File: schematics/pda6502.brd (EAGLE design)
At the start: 100 x 80 mm, 38 parts, among them IC1 74HC00D, IC2 74HC138D, IC3 DS1813-SMD, J1 CON_HEADER_2X07-PTH, U1 W65C02S, U2 W65C22S, U3 28C256, U4 UM61256AK-12

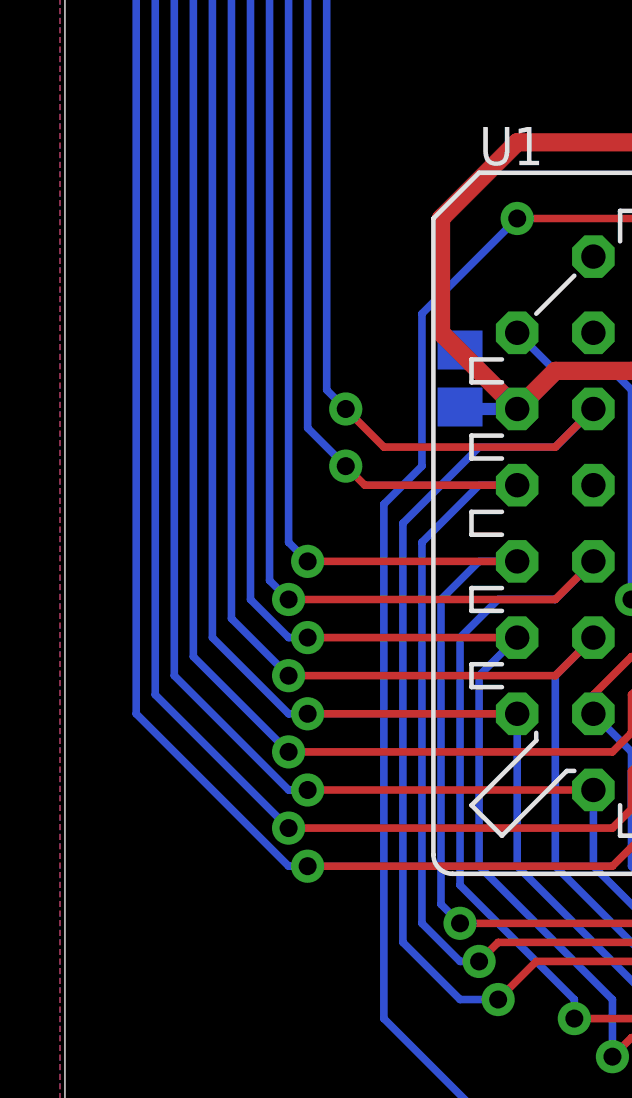
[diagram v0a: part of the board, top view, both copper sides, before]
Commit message: board: PDA6502-LOGO next to 6502.
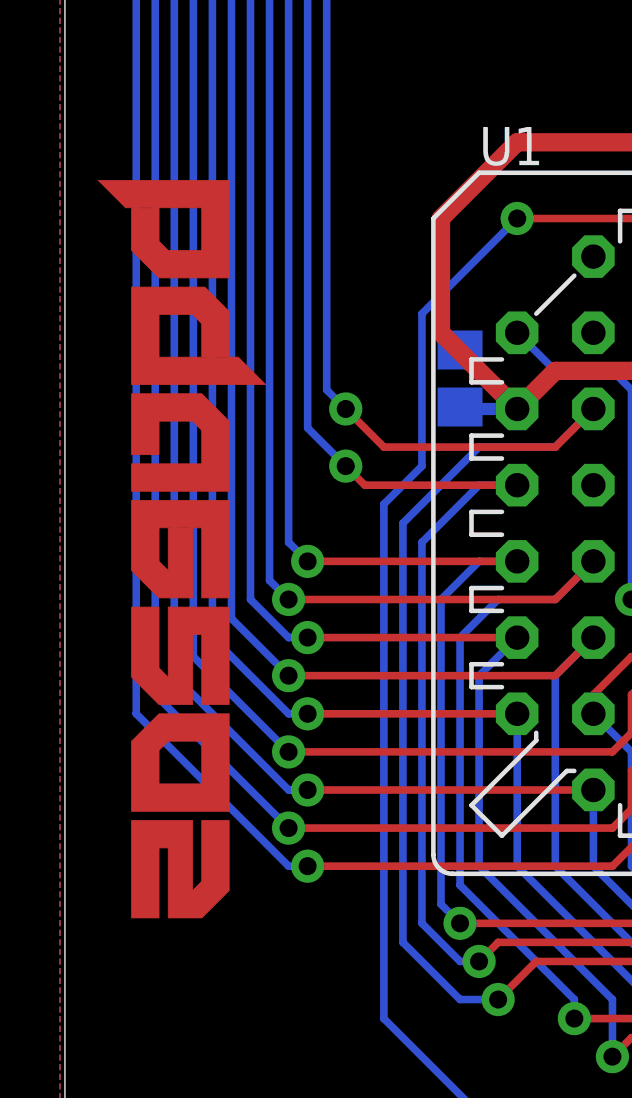
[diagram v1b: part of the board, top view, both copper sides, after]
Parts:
- added U$3: (no value), pda:PDA6502-LOGO
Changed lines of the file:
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@@
 <element name="R4" library="resistor" package="R0805" value="3.3K" x="22.86" y="24.765" rot="MR0"/>
 <element name="U$2" library="pda" package="ADA-TFT-240X230-22INCH" value="" x="67.31" y="27.94"/>
+<element name="U$3" library="pda" package="PDA6502-LOGO" value="" x="1.27" y="36.83" rot="R270"/>
 </elements>
 <signals>

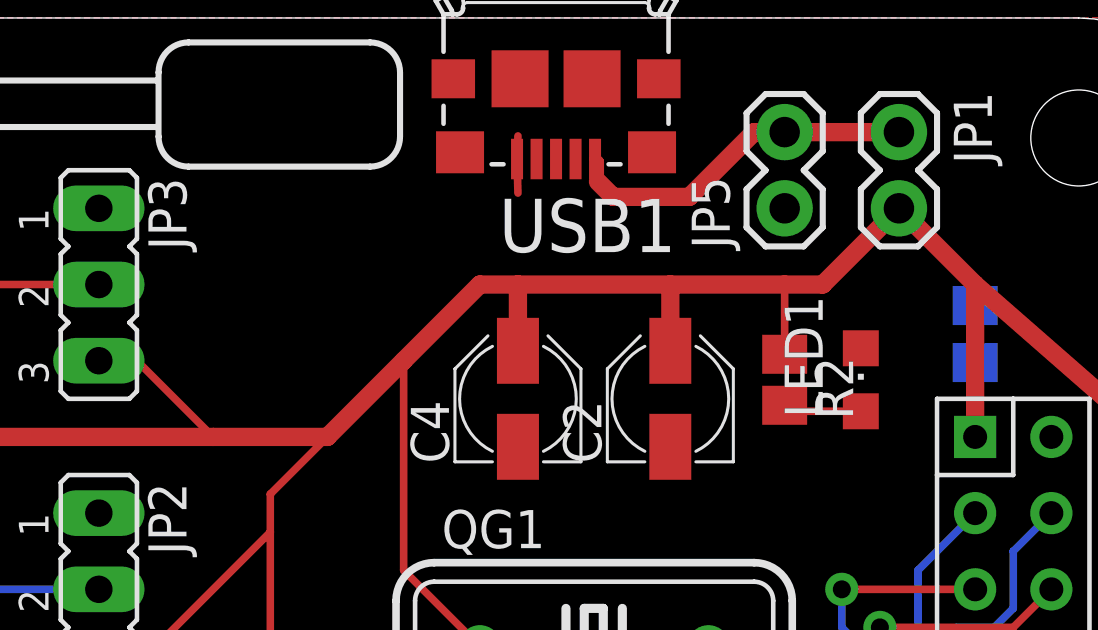
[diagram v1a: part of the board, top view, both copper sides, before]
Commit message: board: PDA6502-LOGO on bottom also; near USB connector.
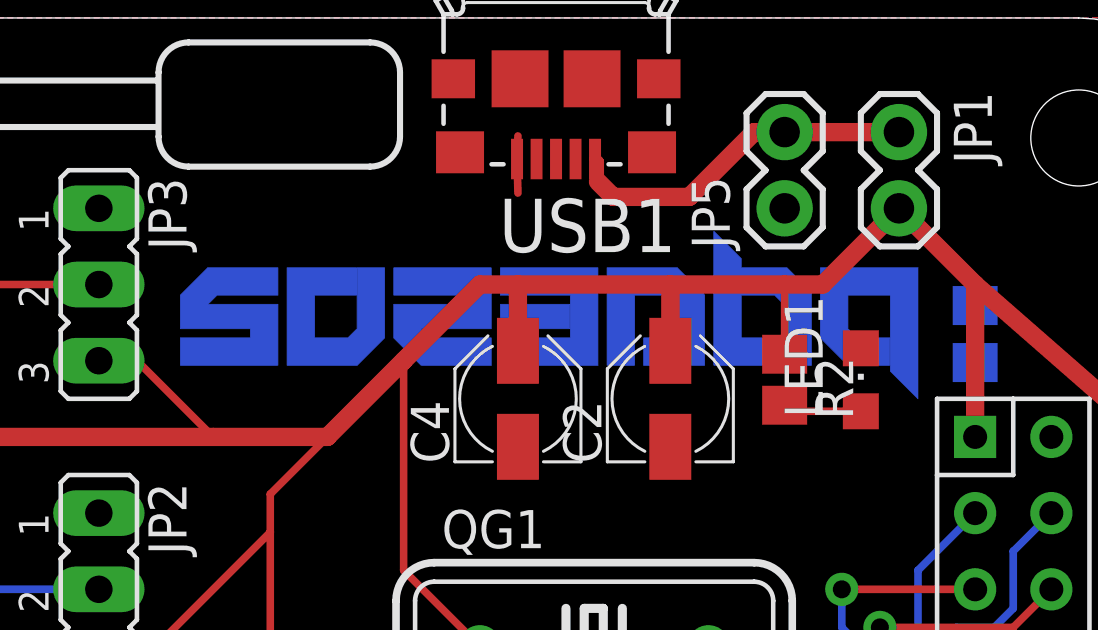
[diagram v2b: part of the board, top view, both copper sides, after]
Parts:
- added U$4: (no value), pda:PDA6502-LOGO
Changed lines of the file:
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@@
 <element name="U$2" library="pda" package="ADA-TFT-240X230-22INCH" value="" x="67.31" y="27.94"/>
 <element name="U$3" library="pda" package="PDA6502-LOGO" value="" x="1.27" y="36.83" rot="R270"/>
+<element name="U$4" library="pda" package="PDA6502-LOGO" value="" x="90.805" y="67.31" rot="MR0"/>
 </elements>
 <signals>

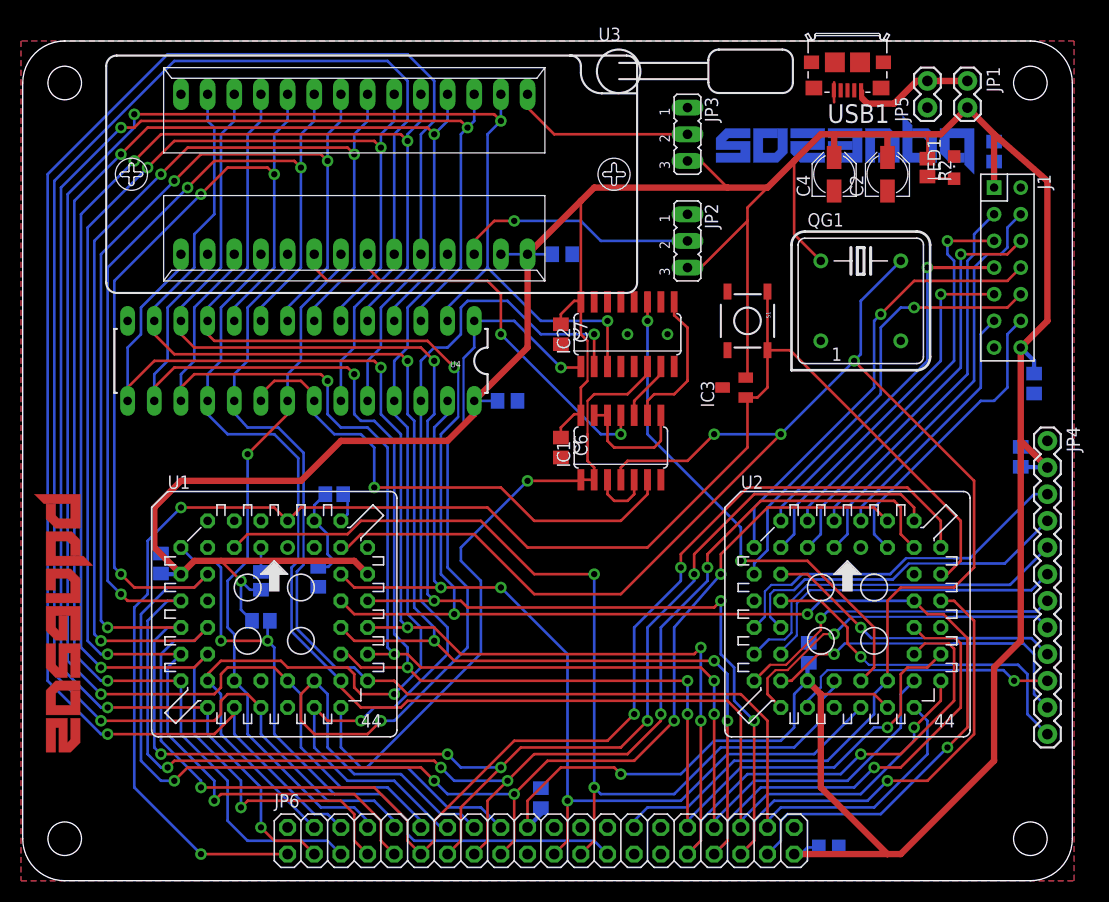
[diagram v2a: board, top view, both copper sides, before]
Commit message: schematics, board: labelling WIP, bigger caps.
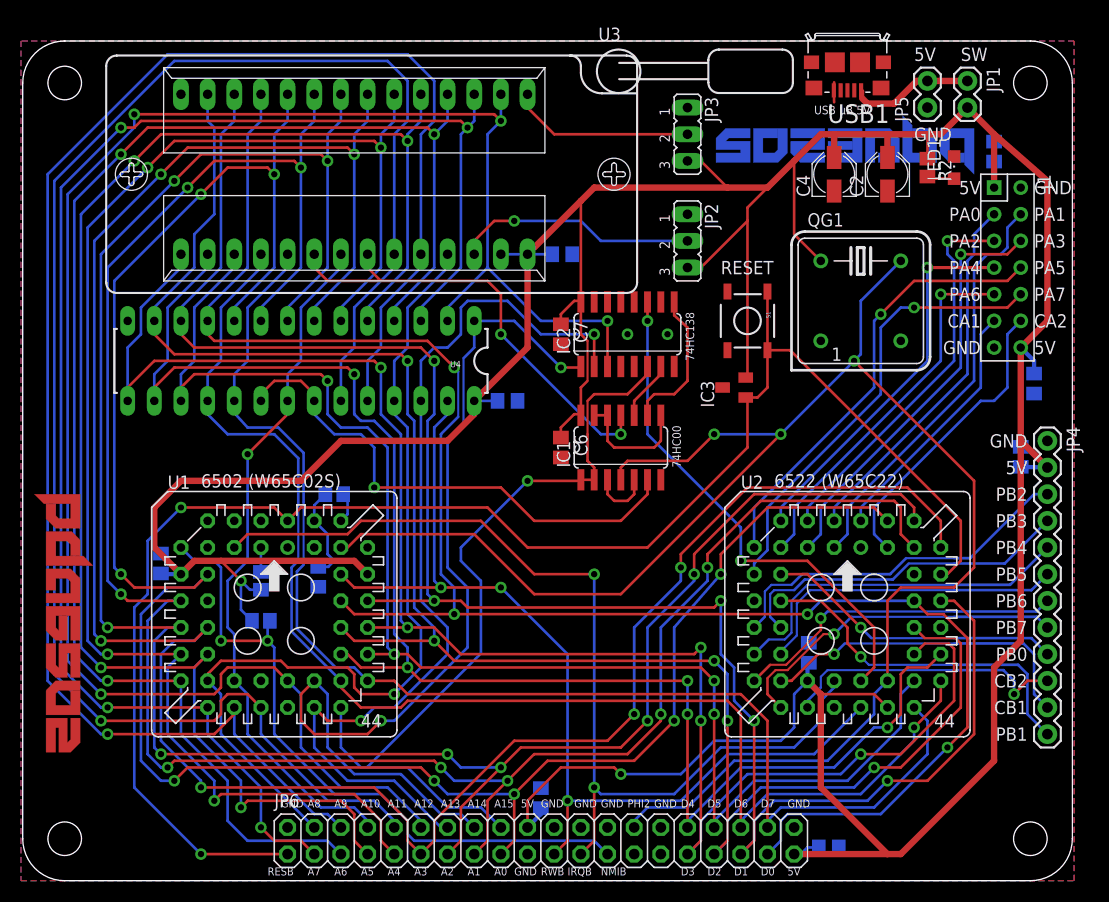
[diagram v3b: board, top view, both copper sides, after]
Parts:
- C12, C13, C14, C9: value 0.1μF -> 1μF
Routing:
- net CB2: track 25.7 -> 27.5 mm
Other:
- board text added: "5V"
- board text added: "6502 (W65C02S)"
- board text added: "6522 (W65C22)"
- board text added: "74HC00"
- board text added: "74HC138"
- board text added: "A0"
- board text added: "A1"
- board text added: "A10"
- board text added: "A11"
- board text added: "A12"
- board text added: "A13"
- board text added: "A14"
- board text added: "A15"
- board text added: "A2"
- board text added: "A3"
- board text added: "A4"
- board text added: "A5"
- board text added: "A6"
- board text added: "A7"
- board text added: "A8"
- board text added: "A9"
- board text added: "CA1"
- board text added: "CA2"
- board text added: "CB1"
- board text added: "CB2"
- board text added: "D0"
- board text added: "D1"
- board text added: "D2"
- board text added: "D3"
- board text added: "D4"
- board text added: "D5"
- board text added: "D6"
- board text added: "D7"
- board text added: "GND"
- board text added: "IRQB"
- board text added: "NMIB"
- board text added: "PA0"
- board text added: "PA1"
- board text added: "PA2"
- board text added: "PA3"
- board text added: "PA4"
- board text added: "PA5"
- board text added: "PA6"
- board text added: "PA7"
- board text added: "PB0"
- board text added: "PB1"
- board text added: "PB2"
- board text added: "PB3"
- board text added: "PB4"
- board text added: "PB5"
- board text added: "PB6"
- board text added: "PB7"
- board text added: "PHI2"
- board text added: "RESB"
- board text added: "RESET"
- board text added: "RWB"
- board text added: "SW"
- board text added: "USB µB 5V"
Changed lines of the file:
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@@
 <board>
 <plain>
+<text x="24.765" y="6.985" size="0.762" layer="21" font="vector">GND</text>
+<text x="46.99" y="1.27" size="0.762" layer="21" font="vector" align="top-left">GND</text>
+<text x="49.53" y="6.985" size="0.762" layer="21" font="vector">GND</text>
+<text x="52.705" y="6.985" size="0.762" layer="21" font="vector">GND</text>
+<text x="55.245" y="6.985" size="0.762" layer="21" font="vector">GND</text>
+<text x="60.325" y="6.985" size="0.762" layer="21" font="vector">GND</text>
+<text x="73.025" y="6.985" size="0.762" layer="21" font="vector">GND</text>
+<text x="47.625" y="6.985" size="0.762" layer="21" font="vector">5V</text>
+<text x="73.025" y="1.27" size="0.762" layer="21" font="vector" align="top-left">5V</text>
+<text x="23.495" y="1.27" size="0.762" layer="21" font="vector" align="top-left">RESB</text>
+<text x="27.305" y="1.27" size="0.762" layer="21" font="vector" align="top-left">A7</text>
+<text x="29.845" y="1.27" size="0.762" layer="21" font="vector" align="top-left">A6</text>
+<text x="32.385" y="1.27" size="0.762" layer="21" font="vector" align="top-left">A5</text>
+<text x="34.925" y="1.27" size="0.762" layer="21" font="vector" align="top-left">A4</text>
+<text x="37.465" y="1.27" size="0.762" layer="21" font="vector" align="top-left">A3</text>
+<text x="40.005" y="1.27" size="0.762" layer="21" font="vector" align="top-left">A2</text>
+<text x="42.545" y="1.27" size="0.762" layer="21" font="vector" align="top-left">A1</text>
+<text x="45.085" y="1.27" size="0.762" layer="21" font="vector" align="top-left">A0</text>
+<text x="27.305" y="6.985" size="0.762" layer="21" font="vector">A8</text>
+<text x="29.845" y="6.985" size="0.762" layer="21" font="vector">A9</text>
+<text x="32.385" y="6.985" size="0.762" layer="21" font="vector">A10</text>
+<text x="34.925" y="6.985" size="0.762" layer="21" font="vector">A11</text>
+<text x="37.465" y="6.985" size="0.762" layer="21" font="vector">A12</text>
+<text x="40.005" y="6.985" size="0.762" layer="21" font="vector">A13</text>
+<text x="42.545" y="6.985" size="0.762" layer="21" font="vector">A14</text>
+<text x="45.085" y="6.985" size="0.762" layer="21" font="vector">A15</text>
+<text x="70.485" y="1.27" size="0.762" layer="21" font="vector" align="top-left">D0</text>
+<text x="67.945" y="1.27" size="0.762" layer="21" font="vector" align="top-left">D1</text>
+<text x="65.405" y="1.27" size="0.762" layer="21" font="vector" align="top-left">D2</text>
+<text x="62.865" y="1.27" size="0.762" layer="21" font="vector" align="top-left">D3</text>
+<text x="62.865" y="6.985" size="0.762" layer="21" font="vector">D4</text>
+<text x="65.405" y="6.985" size="0.762" layer="21" font="vector">D5</text>
+<text x="67.945" y="6.985" size="0.762" layer="21" font="vector">D6</text>
+<text x="70.485" y="6.985" size="0.762" layer="21" font="vector">D7</text>
+<text x="49.53" y="1.27" size="0.762" layer="21" font="vector" align="top-left">RWB</text>
+<text x="52.07" y="1.27" size="0.762" layer="21" font="vector" align="top-left">IRQB</text>
+<text x="55.245" y="1.27" size="0.762" layer="21" font="vector" align="top-left">NMIB</text>
+<text x="57.785" y="6.985" size="0.762" layer="21" font="vector">PHI2</text>
+<text x="95.885" y="41.275" size="1.27" layer="21" font="vector" align="bottom-right">GND</text>
+<text x="95.885" y="38.735" size="1.27" layer="21" font="vector" align="bottom-right">5V</text>
+<text x="95.885" y="36.195" size="1.27" layer="21" font="vector" align="bottom-right">PB2</text>
+<text x="95.885" y="33.655" size="1.27" layer="21" font="vector" align="bottom-right">PB3</text>
+<text x="95.885" y="31.115" size="1.27" layer="21" font="vector" align="bottom-right">PB4</text>
+<text x="95.885" y="28.575" size="1.27" layer="21" font="vector" align="bottom-right">PB5</text>
+<text x="95.885" y="26.035" size="1.27" layer="21" font="vector" align="bottom-right">PB6</text>
+<text x="95.885" y="23.495" size="1.27" layer="21" font="vector" align="bottom-right">PB7</text>
+<text x="95.885" y="20.955" size="1.27" layer="21" font="vector" align="bottom-right">PB0</text>
+<text x="95.885" y="18.415" size="1.27" layer="21" font="vector" align="bottom-right">CB2</text>
+<text x="95.885" y="15.875" size="1.27" layer="21" font="vector" align="bottom-right">CB1</text>
+<text x="95.885" y="13.335" size="1.27" layer="21" font="vector" align="bottom-right">PB1</text>
+<text x="91.44" y="50.165" size="1.27" layer="21" font="vector" align="bottom-right">GND</text>
+<text x="91.44" y="65.405" size="1.27" layer="21" font="vector" align="bottom-right">5V</text>
+<text x="91.44" y="62.865" size="1.27" layer="21" font="vector" align="bottom-right">PA0</text>
+<text x="91.44" y="60.325" size="1.27" layer="21" font="vector" align="bottom-right">PA2</text>
+<text x="91.44" y="57.785" size="1.27" layer="21" font="vector" align="bottom-right">PA4</text>
+<text x="91.44" y="55.245" size="1.27" layer="21" font="vector" align="bottom-right">PA6</text>
+<text x="91.44" y="52.705" size="1.27" layer="21" font="vector" align="bottom-right">CA1</text>
+<text x="96.52" y="65.405" size="1.27" layer="21" font="vector">GND</text>
+<text x="96.52" y="62.865" size="1.27" layer="21" font="vector">PA1</text>
+<text x="96.52" y="60.325" size="1.27" layer="21" font="vector">PA3</text>
+<text x="96.52" y="57.785" size="1.27" layer="21" font="vector">PA5</text>
+<text x="96.52" y="55.245" size="1.27" layer="21" font="vector">PA7</text>
+<text x="96.52" y="52.705" size="1.27" layer="21" font="vector">CA2</text>
+<text x="96.52" y="50.165" size="1.27" layer="21" font="vector">5V</text>
+<text x="66.675" y="57.785" size="1.27" layer="21" font="vector">RESET</text>
+<text x="75.565" y="73.025" size="0.8128" layer="21" font="vector">USB µB 5V</text>
+<text x="85.09" y="78.105" size="1.27" layer="21" font="vector">5V</text>
+<text x="89.535" y="78.105" size="1.27" layer="21" font="vector">SW</text>
+<text x="85.09" y="70.485" size="1.27" layer="21" font="vector">GND</text>
+<text x="17.145" y="37.465" size="1.27" layer="21" font="vector">6502 (W65C02S)</text>
+<text x="71.755" y="37.465" size="1.27" layer="21" font="vector">6522 (W65C22)</text>
+<text x="62.865" y="39.37" size="0.8128" layer="21" font="vector" rot="R90">74HC00</text>
+<text x="64.135" y="49.53" size="0.8128" layer="21" font="vector" rot="R90">74HC138</text>
 </plain>
 <attributes>
@@
 <element name="C10" library="rcl" package="C0805" value="0.1μF" x="46.355" y="45.72" rot="MR180"/>
 <element name="C11" library="rcl" package="C0805" value="0.1μF" x="92.71" y="69.469" rot="MR90"/>
-<element name="C12" library="rcl" package="C0805" value="0.1μF" x="96.52" y="47.371" rot="MR270"/>
+<element name="C12" library="rcl" package="C0805" value="1μF" x="96.52" y="47.371" rot="MR270"/>
 <element name="C2" library="dangerousprototypes_devices" package="CASE_B" value="47uF" x="82.55" y="67.31" rot="R90"/>
 <element name="C3" library="rcl" package="C0805" value="0.1μF" x="28.321" y="28.956" rot="MR270"/>
@@
 <element name="C7" library="rcl" package="C0805" value="0.1μF" x="51.435" y="52.07" rot="R270"/>
 <element name="C8" library="rcl" package="C0805" value="0.1μF" x="51.562" y="59.69" rot="MR180"/>
-<element name="C9" library="rcl" package="C0805" value="0.1μF" x="95.25" y="40.386" rot="MR90"/>
+<element name="C9" library="rcl" package="C0805" value="1μF" x="95.25" y="40.386" rot="MR90"/>
 <element name="IC1" library="74xx-eu" package="SO14" value="74HC00D" x="57.15" y="41.275"/>
 <element name="IC2" library="74xx-eu" package="SO16" value="74HC138D" x="57.785" y="52.07"/>
@@
 <element name="JP5" library="SparkFun-Connectors" package="1X02" value="EXT5V" x="86.36" y="73.66" rot="R90"/>
 <element name="JP6" library="adafruit" package="2X20" value="EXPANSION" x="49.53" y="3.81"/>
-<element name="C13" library="rcl" package="C0805" value="0.1μF" x="76.962" y="3.175" rot="MR0"/>
-<element name="C14" library="rcl" package="C0805" value="0.1μF" x="49.53" y="7.874" rot="MR270"/>
+<element name="C13" library="rcl" package="C0805" value="1μF" x="76.962" y="3.175" rot="MR0"/>
+<element name="C14" library="rcl" package="C0805" value="1μF" x="49.53" y="7.874" rot="MR270"/>
 <element name="R3" library="resistor" package="R0805" value="3.3K" x="29.845" y="36.83" rot="MR0"/>
 <element name="R4" library="resistor" package="R0805" value="3.3K" x="22.86" y="24.765" rot="MR0"/>
@@
 <contactref element="U2" pad="20"/>
 <contactref element="JP4" pad="10"/>
-<wire x1="97.79" y1="19.05" x2="94.615" y2="19.05" width="0.254" layer="1"/>
-<via x="94.615" y="19.05" extent="1-16" drill="0.6"/>
+<wire x1="97.79" y1="19.05" x2="95.885" y2="19.05" width="0.254" layer="1"/>
+<wire x1="95.885" y1="19.05" x2="94.615" y2="17.78" width="0.254" layer="1"/>
+<via x="94.615" y="17.78" extent="1-16" drill="0.6"/>
 <wire x1="76.2" y1="18.415" x2="76.2" y2="19.431" width="0.2032" layer="16"/>
 <wire x1="76.2" y1="18.415" x2="74.93" y2="17.145" width="0.254" layer="16"/>
@@
 <wire x1="88.9" y1="20.066" x2="93.599" y2="20.066" width="0.254" layer="16"/>
 <wire x1="93.599" y1="20.066" x2="94.615" y2="19.05" width="0.254" layer="16"/>
+<wire x1="94.615" y1="19.05" x2="94.615" y2="17.78" width="0.254" layer="16"/>
 </signal>
 <signal name="RWB">
